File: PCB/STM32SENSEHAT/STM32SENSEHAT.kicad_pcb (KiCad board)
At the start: 2 copper layers, 7.5 x 2 mm, 90 parts, among them IC1 DW01A, J1 USB_B_Micro, J10 Conn_01x01_Pin, J11 Conn_01x02_Pin, J12 Conn_01x04_Pin, J13 Conn_01x04_Pin, J2 Conn_01x24_Socket, J3 Conn_01x24_Socket, J4 Conn_01x05_Pin, J5 Conn_01x24_Pin, J6 Conn_01x10_Pin, J7 Conn_01x04_Socket, J8 Conn_01x24_Pin, J9 Conn_01x05_Socket, Q1 AO3401A, SW1 SW_Push, U1 MCP1700x-330xxTT, U2 TP4056, U3 FT230XQ, U4 BME280, U5 CAT24C256, U6 LTR-303ALS-01, U7 8205A

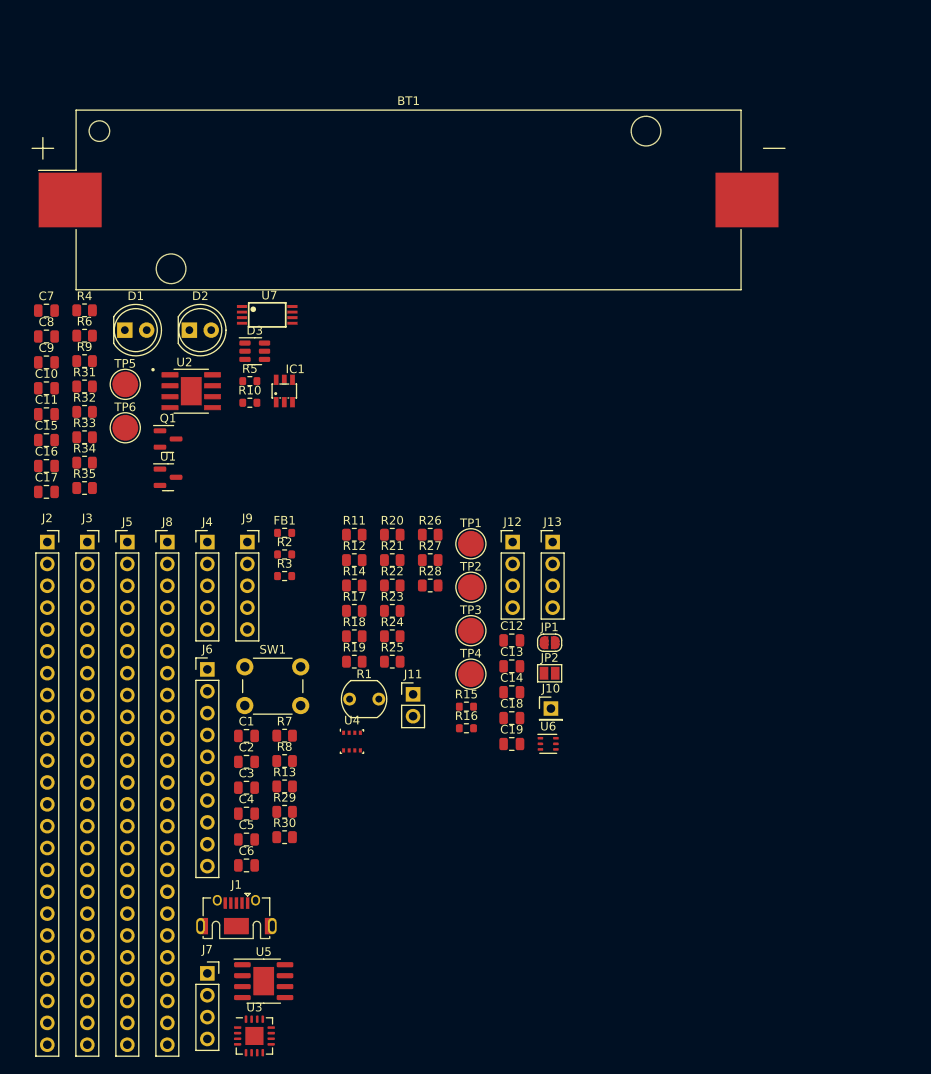
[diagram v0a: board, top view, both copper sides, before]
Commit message: Rework of Power,MCU and Sensor Schematic
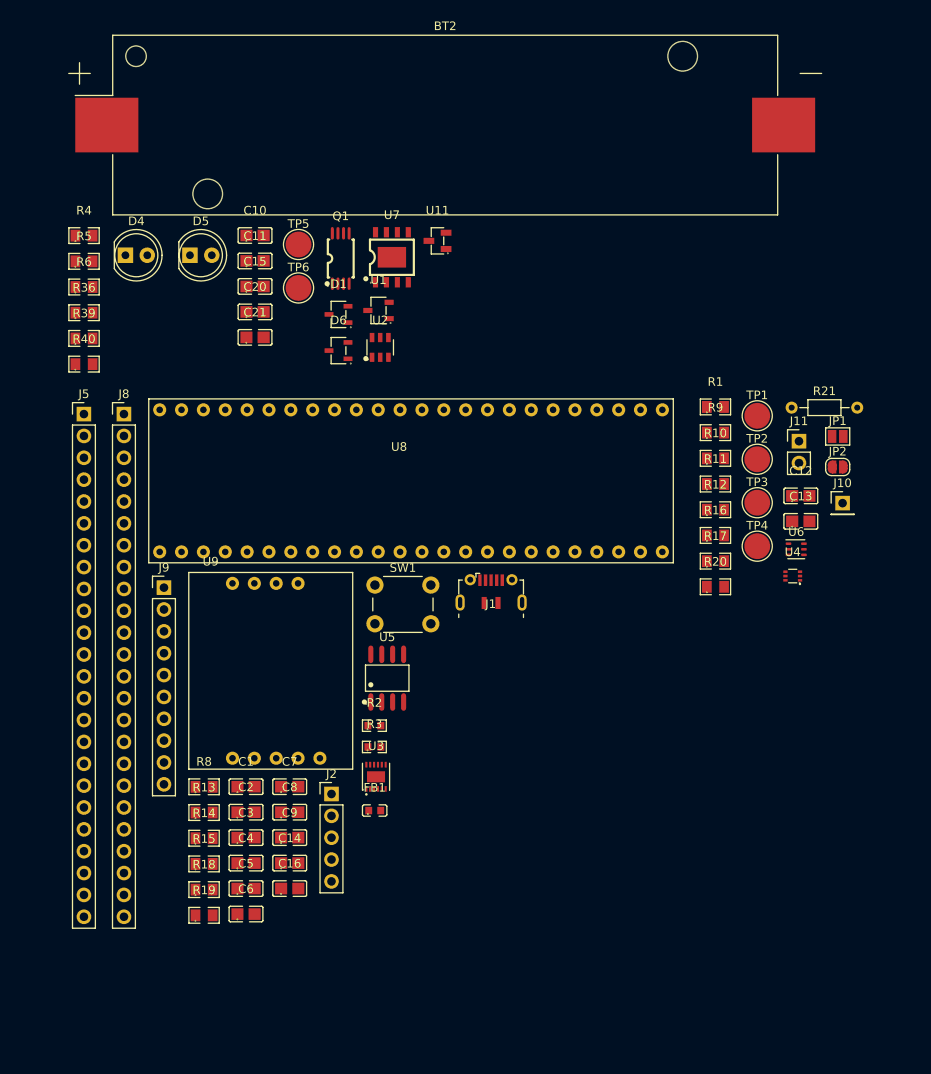
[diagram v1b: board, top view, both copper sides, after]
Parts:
- removed BT1: Battery_Cell, Battery:BatteryHolder_Keystone_1042_1x18650
- removed C17: 1uF, Capacitor_SMD:C_0805_2012Metric
- removed C18, C19: 100nF, Capacitor_SMD:C_0805_2012Metric
- removed D2: LED, LED_THT:LED_D5.0mm
- removed D3: D_Schottky, Package_TO_SOT_SMD:TSOT-23-6
- removed IC1: DW01A, DW01A:SOT23-6
- removed J12, J13: Conn_01x04_Pin, Connector_PinHeader_2.54mm:PinHeader_1x04_P2.54mm_Vertical
- removed J3: Conn_01x24_Socket, Connector_PinSocket_2.54mm:PinSocket_1x24_P2.54mm_Vertical
- removed J4: Conn_01x05_Pin, Connector_PinHeader_2.54mm:PinHeader_1x05_P2.54mm_Vertical
- removed J6: Conn_01x10_Pin, Connector_PinHeader_2.54mm:PinHeader_1x10_P2.54mm_Vertical
- removed J7: Conn_01x04_Socket, Connector_PinSocket_2.54mm:PinSocket_1x04_P2.54mm_Vertical
- removed R22, R23, R24, R25, R26, R27, R28, R29, R30, R31, R32, R33, R34: 0R, Resistor_SMD:R_0805_2012Metric
- removed R35, R7: 10k, Resistor_SMD:R_0805_2012Metric
- added BT2: Battery_Cell, Battery:BatteryHolder_Keystone_1042_1x18650, F.Cu at (147.5, 37.5)
- added C20: 10uF, JLCfootprint:C0805, F.Cu at (125.4, 59.2)
- added C21: 10uF, JLCfootprint:C0805, F.Cu at (125.4, 62.2)
- added D4: LED, LED_THT:LED_D5.0mm, F.Cu at (110.3, 52.6)
- added D5: LED, LED_THT:LED_D5.0mm, F.Cu at (117.8, 52.6)
- added D6: D_Schottky, JLCfootprint:SOT-23-3_L3.0-W1.7-P0.95-LS2.9-BR, F.Cu at (135.1, 63.7)
- added R36: 10k, JLCfootprint:R0805, F.Cu at (105.5, 59.3)
- added R39: 0R, JLCfootprint:R0805, F.Cu at (105.5, 62.3)
- added R40: 1k0, JLCfootprint:R0805, F.Cu at (105.5, 65.3)
- added U11: AO3401A_C306862, JLCfootprint:SOT-23-3_L2.9-W1.3-P1.90-LS2.4-BR, F.Cu at (146.6, 51.0)
- added U8: ~, footprints:STM32F051C6T6, F.Cu at (142.3, 81.0)
- added U9: STLINK_UCT, footprints:STLINK_UCT, F.Cu at (126.6, 100.9)
- C1, C10, C11, C2, C3, C4, C5, C6, C9: footprint Capacitor_SMD:C_0805_2012Metric -> JLCfootprint:C0805
- C12: value 100nF -> 1uF; footprint Capacitor_SMD:C_0805_2012Metric -> JLCfootprint:C0805
- C13: value 100nF -> 10nF; footprint Capacitor_SMD:C_0805_2012Metric -> JLCfootprint:C0805
- C14, C15: value 1uF -> 10nF; footprint Capacitor_SMD:C_0805_2012Metric -> JLCfootprint:C0805
- C16: value 1uF -> 4.7uF; footprint Capacitor_SMD:C_0805_2012Metric -> JLCfootprint:C0805
- C7: value 10uF -> 1uF; footprint Capacitor_SMD:C_0805_2012Metric -> JLCfootprint:C0805
- C8: value 10uF -> 100nF; footprint Capacitor_SMD:C_0805_2012Metric -> JLCfootprint:C0805
- D1: value LED -> D_Schottky; footprint LED_THT:LED_D5.0mm -> JLCfootprint:SOT-23-3_L3.0-W1.7-P0.95-LS2.9-BR
- FB1: footprint Resistor_SMD:R_0603_1608Metric -> JLCfootprint:L0603
- J1: footprint Connector_USB:USB_Micro-AB_Molex_47590-0001 -> footprints:USB_Conn_JLC_LCSC_C404969
- J2: value Conn_01x24_Socket -> Conn_01x05_Pin; footprint Connector_PinSocket_2.54mm:PinSocket_1x24_P2.54mm_Vertical -> Connector_PinHeader_2.54mm:PinHeader_1x05_P2.54mm_Vertical
- J9: value Conn_01x05_Socket -> Conn_01x10_Pin; footprint Connector_PinSocket_2.54mm:PinSocket_1x05_P2.54mm_Vertical -> Connector_PinHeader_2.54mm:PinHeader_1x10_P2.54mm_Vertical
- JP1: footprint Jumper:SolderJumper-2_P1.3mm_Open_RoundedPad1.0x1.5mm -> Jumper:SolderJumper-2_P1.3mm_Open_Pad1.0x1.5mm
- JP2: footprint Jumper:SolderJumper-2_P1.3mm_Open_Pad1.0x1.5mm -> Jumper:SolderJumper-2_P1.3mm_Open_RoundedPad1.0x1.5mm
- Q1: value AO3401A -> FS8205A; footprint Package_TO_SOT_SMD:SOT-23 -> JLCfootprint:TSSOP-8_L4.4-W3.0-P0.65-LS6.4-BL
- R1: value LDR07 -> 0R; footprint OptoDevice:R_LDR_5.1x4.3mm_P3.4mm_Vertical -> JLCfootprint:R0805
- R10: value 1k -> 0R; footprint Resistor_SMD:R_0603_1608Metric -> JLCfootprint:R0805
- R11, R12: value 4k7 -> 0R; footprint Resistor_SMD:R_0805_2012Metric -> JLCfootprint:R0805
- R13, R8: value 1.5k -> 0R; footprint Resistor_SMD:R_0805_2012Metric -> JLCfootprint:R0805
- R14: footprint Resistor_SMD:R_0805_2012Metric -> JLCfootprint:R0805
- R15: value 1k0 -> 4k7; footprint Resistor_SMD:R_0603_1608Metric -> JLCfootprint:R0805
- R16: value 1k0 -> 0R; footprint Resistor_SMD:R_0603_1608Metric -> JLCfootprint:R0805
- R17: value 10k -> 0R; footprint Resistor_SMD:R_0805_2012Metric -> JLCfootprint:R0805
- R18: value 0R -> 4k7; footprint Resistor_SMD:R_0805_2012Metric -> JLCfootprint:R0805
- R19, R20: value 0R -> 10k; footprint Resistor_SMD:R_0805_2012Metric -> JLCfootprint:R0805
- R2, R3: footprint Resistor_SMD:R_0603_1608Metric -> JLCfootprint:R0603
- R21: value 0R -> LDR07; footprint Resistor_SMD:R_0805_2012Metric -> Resistor_THT:R_Axial_DIN0204_L3.6mm_D1.6mm_P7.62mm_Horizontal
- R4: value 0.4R -> 1k0; footprint Resistor_SMD:R_0805_2012Metric -> JLCfootprint:R0805
- R5: value 1k0 -> 10k; footprint Resistor_SMD:R_0603_1608Metric -> JLCfootprint:R0805
- R6: value 10k -> 100R; footprint Resistor_SMD:R_0805_2012Metric -> JLCfootprint:R0805
- R9: value 100R -> 0R; footprint Resistor_SMD:R_0805_2012Metric -> JLCfootprint:R0805
- U1: footprint Package_TO_SOT_SMD:SOT-23 -> JLCfootprint:SOT-23-3_L2.9-W1.6-P1.90-LS2.8-BR
- U2: value TP4056 -> ~; footprint TP4056:SOP127P600X175-9N -> JLCfootprint:SOT-23-6_L2.9-W1.6-P0.95-LS2.8-BL
- U3: value FT230XQ -> FT234XD-R; footprint Package_DFN_QFN:QFN-16-1EP_4x4mm_P0.65mm_EP2.1x2.1mm -> JLCfootprint:DFN-12_L3.0-W3.0-P0.45-BL-EP
- U4: value BME280 -> TMP102xxDRL; footprint Package_LGA:Bosch_LGA-8_2.5x2.5mm_P0.65mm_ClockwisePinNumbering -> JLCfootprint:SOT-563_L1.6-W1.2-P0.50-LS1.6-BR
- U5: footprint Package_SO:SOIC-8-1EP_3.9x4.9mm_P1.27mm_EP2.41x3.3mm -> JLCfootprint:SOIC-8_L4.9-W3.9-P1.27-LS6.0-BL
- U7: value 8205A -> ~; footprint 8205A:TSSOP8 -> JLCfootprint:ESOP-8_L4.9-W3.9-P1.27-LS6.0-BL-EP
- moved R9 73.8 mm to (178.9, 73.3)
- moved C7 62.1 mm to (129.4, 114.4)
- moved C8 62.1 mm to (129.4, 117.4)
- moved C9 62.0 mm to (129.4, 120.3)
- moved C16 56.7 mm to (129.4, 126.3)
- moved U4 54.7 mm to (187.9, 89.9)
- moved R10 54.5 mm to (178.9, 76.2)
- moved R1 54.4 mm to (178.9, 70.3)
- moved J11 53.6 mm to (188.6, 74.3)
- moved R21 49.7 mm to (187.7, 70.4)
- moved J1 47.3 mm to (152.8, 93.7)
- moved J2 44.1 mm to (134.3, 115.3)
- moved R11 42.4 mm to (178.9, 79.2)
- moved R12 42.4 mm to (178.9, 82.2)
- moved R17 42.4 mm to (178.9, 88.2)
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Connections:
- C12 pad 1: GND -> Net-(JP1-A)
- C12 pad 2: Net-(U4-VDDIO) -> GND
- C13 pad 1: GND -> 3V3
- C13 pad 2: Net-(U4-VDD) -> GND
- C14 pad 1: Net-(JP2-A) -> 3V3
- C15 pad 1: 3V3 -> Net-(U2-VDD)
- C15 pad 2: GND -> Net-(D1-K)
- C2 pad 1: /MCU MODULE/VBUS -> /MCU MODULE/PB0
- C7 pad 1: /MCU MODULE/PA4 -> 3V3
- C8 pad 1: Net-(C8-Pad1) -> 3V3
- C9 pad 1: Net-(IC1-VCC) -> 3V3
- D1 pad 2: Net-(D1-A) -> Net-(BT2--)
- FB1 pad 2: /MCU MODULE/VBUS -> /MCU MODULE/PB0
- J1 pad 1: /MCU MODULE/VBUS -> /MCU MODULE/PB0
- J2 pad 1: 3V3 -> /MCU MODULE/PB0
- J2 pad 2: /MCU MODULE/PC13 -> /MCU MODULE/USB_DN
- J2 pad 3: /MCU MODULE/PC14 -> /MCU MODULE/USB_DP
- J2 pad 4: /MCU MODULE/PC15 -> GND
- J2 pad 5: /MCU MODULE/PF0 -> GND
- J5 pad 1: /MCU MODULE/VDD -> 3V3
- J5 pad 10: /MCU MODULE/PB3 -> /MCU MODULE/PA0
- J5 pad 11: /MCU MODULE/PA15 -> /MCU MODULE/PA1
- J5 pad 12: /MCU MODULE/PA14 -> /MCU MODULE/PA2
- J5 pad 13: /MCU MODULE/PF7 -> /MCU MODULE/PA3
- J5 pad 14: /MCU MODULE/PF6 -> /MCU MODULE/PA4
- J5 pad 15: /MCU MODULE/PA13 -> /MCU MODULE/PA5
- J5 pad 16: /MCU MODULE/PA12 -> /MCU MODULE/PA6
- J5 pad 17: /MCU MODULE/PA11 -> /MCU MODULE/PA7
- J5 pad 18: /MCU MODULE/PA10 -> /MCU MODULE/PB0
- J5 pad 19: /MCU MODULE/PA9 -> /MCU MODULE/PB1
- J5 pad 2: GND -> /MCU MODULE/PC13
- J5 pad 20: /MCU MODULE/PA8 -> /MCU MODULE/PB2
- J5 pad 21: /MCU MODULE/PB15 -> /MCU MODULE/PB10
- J5 pad 22: /MCU MODULE/PB14 -> /MCU MODULE/PB11
- J5 pad 23: /MCU MODULE/PB13 -> GND
- J5 pad 24: /MCU MODULE/PB12 -> 3V3
- J5 pad 3: /MCU MODULE/PB9 -> /MCU MODULE/PC14
- J5 pad 4: /MCU MODULE/PB8 -> /MCU MODULE/PC15
- J5 pad 5: /MCU MODULE/BOOT -> /MCU MODULE/PF0
- J5 pad 6: /MCU MODULE/PB7 -> /MCU MODULE/PF1
- J5 pad 7: /MCU MODULE/PB6 -> /MCU MODULE/NRST
- J5 pad 8: /MCU MODULE/PB5 -> GND
- J5 pad 9: /MCU MODULE/PB4 -> 3V3
- J8 pad 1: /MCU MODULE/VBAT -> 3V3
- J8 pad 10: /MCU MODULE/PA0 -> /MCU MODULE/PB3
- J8 pad 11: /MCU MODULE/PA1 -> /MCU MODULE/PA15
- J8 pad 12: /MCU MODULE/PA2 -> /MCU MODULE/PA14
- J8 pad 13: /MCU MODULE/PA3 -> /MCU MODULE/PF7
- J8 pad 14: /MCU MODULE/PA4 -> /MCU MODULE/PF6
- J8 pad 15: /MCU MODULE/ANALOG DATA READ -> /MCU MODULE/PA13
- J8 pad 16: /MCU MODULE/PA6 -> /MCU MODULE/PA12
- J8 pad 17: /MCU MODULE/PA7 -> /MCU MODULE/PA11
- J8 pad 18: /MCU MODULE/PB0 -> /MCU MODULE/PA10
- J8 pad 19: /MCU MODULE/PB1 -> /MCU MODULE/PA9
- J8 pad 2: /MCU MODULE/PC13 -> GND
- J8 pad 20: /MCU MODULE/PB2 -> /MCU MODULE/PA8
- J8 pad 21: /MCU MODULE/PB10 -> /MCU MODULE/PB15
- J8 pad 22: /MCU MODULE/PB11 -> /MCU MODULE/PB14
- J8 pad 23: GND -> /MCU MODULE/PB13
- J8 pad 24: /MCU MODULE/VDD -> /MCU MODULE/PB12
- J8 pad 3: /MCU MODULE/PC14 -> /MCU MODULE/PB9
- J8 pad 4: /MCU MODULE/PC15 -> /MCU MODULE/PB8
- J8 pad 5: /MCU MODULE/PF0 -> /MCU MODULE/BOOT
- J8 pad 6: /MCU MODULE/PF1 -> /MCU MODULE/PB7
- J8 pad 7: /MCU MODULE/NRST -> /MCU MODULE/PB6
- J8 pad 8: GND -> /MCU MODULE/PB5
- J8 pad 9: /MCU MODULE/VDDA -> /MCU MODULE/PB4
- J9 pad 2: 3V3 -> /MCU MODULE/PA5
- J9 pad 3: /MCU MODULE/USB_DP -> /MCU MODULE/PB7
- J9 pad 4: /MCU MODULE/USB_DN -> /MCU MODULE/PB6
- J9 pad 5: GND -> unconnected-(J9-Pin_5-Pad5)
- JP1 pad 1: /MCU MODULE/ANALOG DATA READ -> Net-(JP1-A)
- JP1 pad 2: Net-(J10-Pin_1) -> 3V3
- JP2 pad 1: Net-(JP2-A) -> /MCU MODULE/PA5
- JP2 pad 2: 3V3 -> Net-(J10-Pin_1)
- Q1 pad 1: 5VUSB -> unconnected-(Q1-Pad1)
- Q1 pad 2: /POWER MANAGEMENT MODULE/LOAD_PWR -> Net-(D1-K)
- Q1 pad 3: /MCU MODULE/PA4 -> Net-(D1-K)
- R1 pad 1: /MCU MODULE/ANALOG DATA READ -> Net-(U4-V+)
- R1 pad 2: GND -> 3V3
- R10 pad 1: Net-(IC1-CS) -> Net-(U4-SCL)
- R10 pad 2: /POWER MANAGEMENT MODULE/S2 -> /MCU MODULE/PB6
- R11 pad 1: /MCU MODULE/PF6 -> Net-(U6-VDD)
- R11 pad 2: Net-(U4-VDDIO) -> Net-(JP1-A)
- R12 pad 1: /MCU MODULE/PF7 -> GND
- R12 pad 2: Net-(U4-VDDIO) -> Net-(U6-GND)
- R13 pad 1: 3V3 -> /MCU MODULE/PB7
- R13 pad 2: /MCU MODULE/PF7 -> Net-(U5-SDA)
- R14 pad 1: Net-(U4-SCK) -> 3V3
- R14 pad 2: /MCU MODULE/PF7 -> Net-(U5-VCC)
- R15 pad 1: Net-(JP2-A) -> /MCU MODULE/PB7
- R15 pad 2: /MCU MODULE/PF6 -> 3V3
- R16 pad 1: Net-(JP2-A) -> Net-(U6-SDA)
- R16 pad 2: /MCU MODULE/PF7 -> /MCU MODULE/PB7
- R17 pad 1: 3V3 -> Net-(U6-SCL)
- R17 pad 2: /MCU MODULE/ANALOG DATA READ -> /MCU MODULE/PB6
- R18 pad 1: Net-(U4-SDI) -> /MCU MODULE/PB6
- R18 pad 2: /MCU MODULE/PF6 -> 3V3
- R19 pad 1: Net-(U4-CSB) -> /MCU MODULE/BOOT
- R19 pad 2: Net-(U4-VDDIO) -> GND
- R20 pad 1: Net-(U4-VDDIO) -> 3V3
- R20 pad 2: 3V3 -> /MCU MODULE/PA5
- R21 pad 1: Net-(U4-VDD) -> /MCU MODULE/PA5
- R21 pad 2: 3V3 -> GND
- R4 pad 1: 5VUSB -> Net-(U2-CS)
- R4 pad 2: Net-(C8-Pad1) -> GND
- R5 pad 1: Net-(C8-Pad1) -> 5VUSB
- R5 pad 2: Net-(D1-A) -> GND
- R6 pad 1: /POWER MANAGEMENT MODULE/PROG -> Net-(U2-VDD)
- R6 pad 2: GND -> /POWER MANAGEMENT MODULE/BATT+
- R8 pad 1: 3V3 -> Net-(U5-SCL)
- R8 pad 2: Net-(R30-Pad2) -> /MCU MODULE/PB6
- R9 pad 1: /MCU MODULE/PA4 -> Net-(U4-SDA)
- R9 pad 2: Net-(IC1-VCC) -> /MCU MODULE/PB7
- TP1 pad 1: /MCU MODULE/PF7 -> /MCU MODULE/PB7
- TP2 pad 1: /MCU MODULE/PF6 -> /MCU MODULE/PB6
- TP3 pad 1: /MCU MODULE/PF6 -> /MCU MODULE/PB7
- TP4 pad 1: /MCU MODULE/PF7 -> /MCU MODULE/PB6
- U2 pad 1: unconnected-(U2-TEMP-Pad1) -> Net-(U2-OD)
- U2 pad 2: /POWER MANAGEMENT MODULE/PROG -> Net-(U2-CS)
- U2 pad 3: GND -> Net-(U2-OC)
- U2 pad 4: 5VUSB -> unconnected-(U2-TD-Pad4)
- U2 pad 5: /MCU MODULE/PA4 -> Net-(U2-VDD)
- U3 pad 1: Net-(U3-3V3OUT) -> Net-(U3-USBDM)
- U3 pad 10: 5VUSB -> /MCU MODULE/PA9
- U3 pad 12: unconnected-(U3-CBUS0-Pad12) -> Net-(U3-USBDP)
- U3 pad 2: /MCU MODULE/PA10 -> Net-(U3-3V3OUT)
- U3 pad 3: GND -> Net-(U3-3V3OUT)
- U3 pad 4: unconnected-(U3-~{CTS}-Pad4) -> 5VUSB
- U3 pad 5: unconnected-(U3-CBUS2-Pad5) -> GND
- U3 pad 6: Net-(U3-USBDP) -> unconnected-(U3-CBUS0-Pad6)
- U3 pad 7: Net-(U3-USBDM) -> /MCU MODULE/PA10
- U3 pad 8: Net-(U3-3V3OUT) -> unconnected-(U3-RTS#-Pad8)
- U4 pad 1: /SENSOR MODULE/1 -> Net-(U4-SCL)
- U4 pad 2: Net-(U4-CSB) -> GND
- U4 pad 3: Net-(U4-SDI) -> unconnected-(U4-ALERT-Pad3)
- U4 pad 4: Net-(U4-SCK) -> GND
- U4 pad 5: Net-(U4-SDO) -> Net-(U4-V+)
- U4 pad 6: Net-(U4-VDDIO) -> Net-(U4-SDA)
- U5 pad 5: /MCU MODULE/PF6 -> Net-(U5-SDA)
- U5 pad 8: 3V3 -> Net-(U5-VCC)
- U7 pad 1: Net-(U7-D1) -> GND
- U7 pad 2: Net-(U7-S1) -> /POWER MANAGEMENT MODULE/PROG
- U7 pad 3: Net-(U7-S1_2) -> GND
- U7 pad 4: /POWER MANAGEMENT MODULE/OD -> 5VUSB
- U7 pad 5: /POWER MANAGEMENT MODULE/OC -> /POWER MANAGEMENT MODULE/BATT+
- U7 pad 8: Net-(U7-D1) -> 5VUSB
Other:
- board outline removed

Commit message: PCB draft
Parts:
- added D1: D_Schottky, JLCfootprint:SOT-23-3_L3.0-W1.7-P0.95-LS2.9-BR, F.Cu at (110.2, 107.0)
- C1, C10, C11, C12, C13, C15, C2, C20, C21, C3, C4, C5, C6: footprint JLCfootprint:C0805 -> Capacitor_SMD:C_0805_2012Metric
- C14, C16, C7, C8, C9: footprint JLCfootprint:C0805 -> Capacitor_THT:C_Disc_D5.0mm_W2.5mm_P5.00mm
- R1, R10, R11, R12, R13, R14, R15, R16, R17, R18, R19, R20, R36, R39, R4, R40, R5, R6, R8, R9: footprint JLCfootprint:R0805 -> Resistor_SMD:R_0805_2012Metric
- R2, R3: footprint JLCfootprint:R0603 -> Resistor_SMD:R_0805_2012Metric
- R21: footprint Resistor_THT:R_Axial_DIN0204_L3.6mm_D1.6mm_P7.62mm_Horizontal -> OptoDevice:R_LDR_5.1x4.3mm_P3.4mm_Vertical
- U2: value ~ -> DW01A
- U6: footprint OptoDevice:Lite-On_LTR-303ALS-01 -> JLCfootprint:SOT-363_L2.0-W1.3-P0.65-LS2.1-BL
- U7: value ~ -> TP4056
- moved R19 80.0 mm to (167.0, 65.0)
- moved R8 69.3 mm to (188.3, 122.0), turned to 180 degrees
- moved R15 68.2 mm to (176.5, 86.0)
- moved R18 67.9 mm to (176.5, 89.5)
- moved U9 65.6 mm to (185.8, 72.8), turned to -90 degrees
- moved R13 64.4 mm to (183.7, 121.9)
- moved J9 61.6 mm to (176.4, 94.2)
- moved J8 60.9 mm to (171.0, 68.4)
- moved R14 60.2 mm to (179.2, 127.8), turned to -90 degrees
- moved U11 60.0 mm to (126.0, 107.3)
- moved R5 59.0 mm to (118.1, 111.0), turned to 180 degrees
- moved J1 56.3 mm to (120.1, 139.5)
- moved Q1 56.2 mm to (118.5, 106.6), turned to -90 degrees
- moved R6 54.7 mm to (110.1, 110.8), turned to 180 degrees
- moved C8 52.8 mm to (150.9, 69.1)
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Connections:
- BT2 pad 1: /POWER MANAGEMENT MODULE/BATT+ -> Net-(BT2-+)
- C15 pad 2: Net-(D1-K) -> Net-(BT2--)
- Q1 pad 2: Net-(D1-K) -> Net-(BT2--)
- Q1 pad 3: Net-(D1-K) -> Net-(BT2--)
- U2 pad 6: Net-(D1-K) -> Net-(BT2--)
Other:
- board outline added: 100 x 100 mm

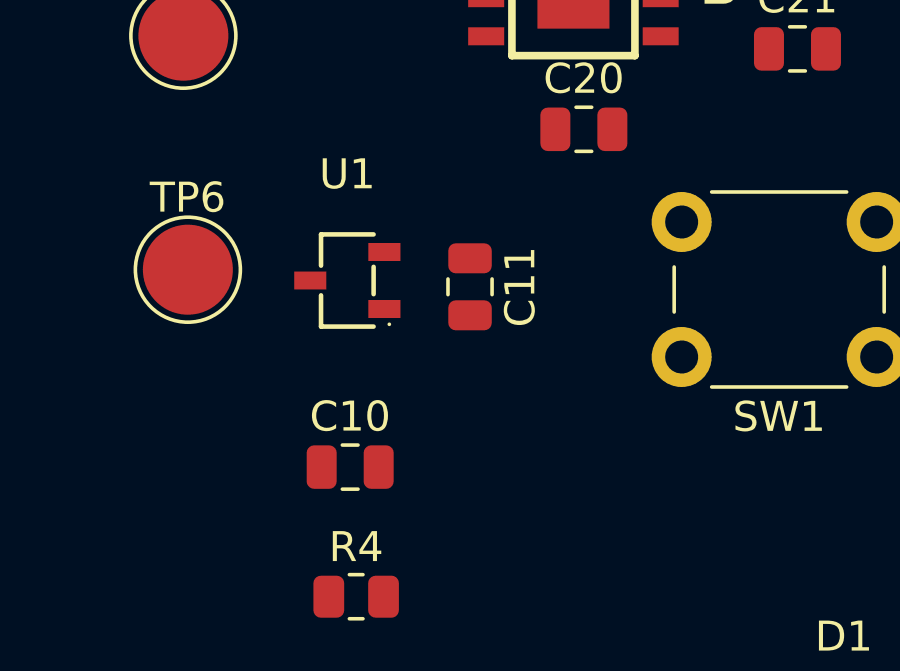
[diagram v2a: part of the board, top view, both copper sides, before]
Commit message: Changed the footprint of cpacitors C10 and C11 to C_disc"
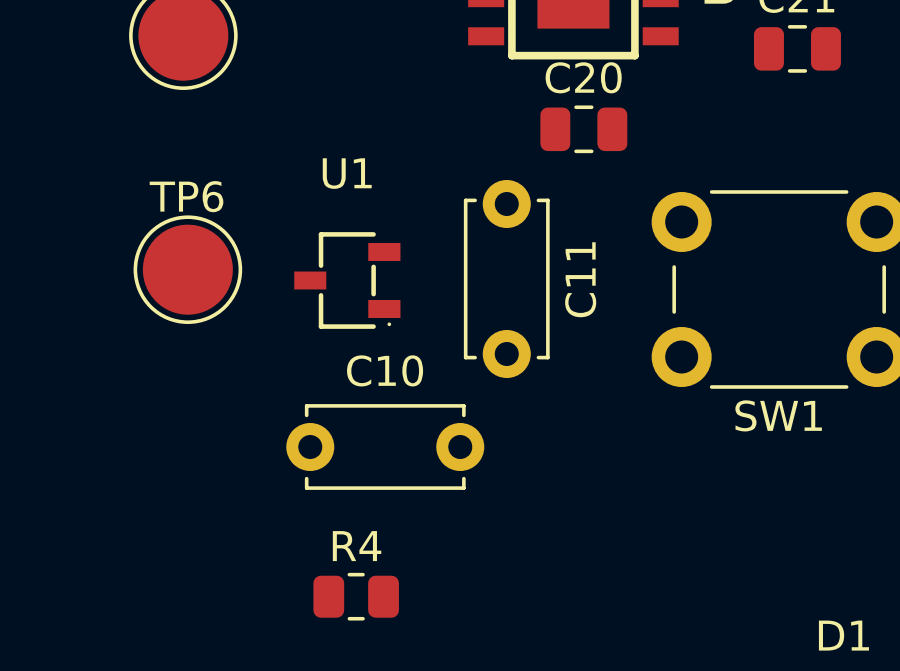
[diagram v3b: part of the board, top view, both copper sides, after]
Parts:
- C10, C11: footprint Capacitor_SMD:C_0805_2012Metric -> Capacitor_THT:C_Disc_D5.0mm_W2.5mm_P5.00mm
- moved C11 3.02 mm to (120.3, 83.7)
- moved C10 1.49 mm to (113.7, 91.8)

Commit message: Update
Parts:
- moved TP1 15.0 mm to (181.7, 96.5)
- moved FB1 14.6 mm to (111.9, 135.4), turned to 180 degrees
- moved C10 8.46 mm to (120.5, 96.9), turned to 90 degrees
- moved R6 8.08 mm to (109.3, 102.8)
- moved C6 5.13 mm to (111.8, 126.5)
- moved C2 4.76 mm to (112.0, 137.8)
- moved C4 4.19 mm to (111.7, 122.9)
- moved C5 4.19 mm to (111.7, 120.0)
- moved C20 3.50 mm to (126.4, 81.4)
- moved R2 3.12 mm to (117.8, 126.2)
- moved R3 2.89 mm to (117.9, 129.4)
- moved C1 2.82 mm to (111.9, 133.2)
- moved J2 2.21 mm to (118.7, 119.3)
- moved R4 2.11 mm to (116.0, 94.8), turned to 90 degrees
- moved R5 1.64 mm to (118.7, 112.5)
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
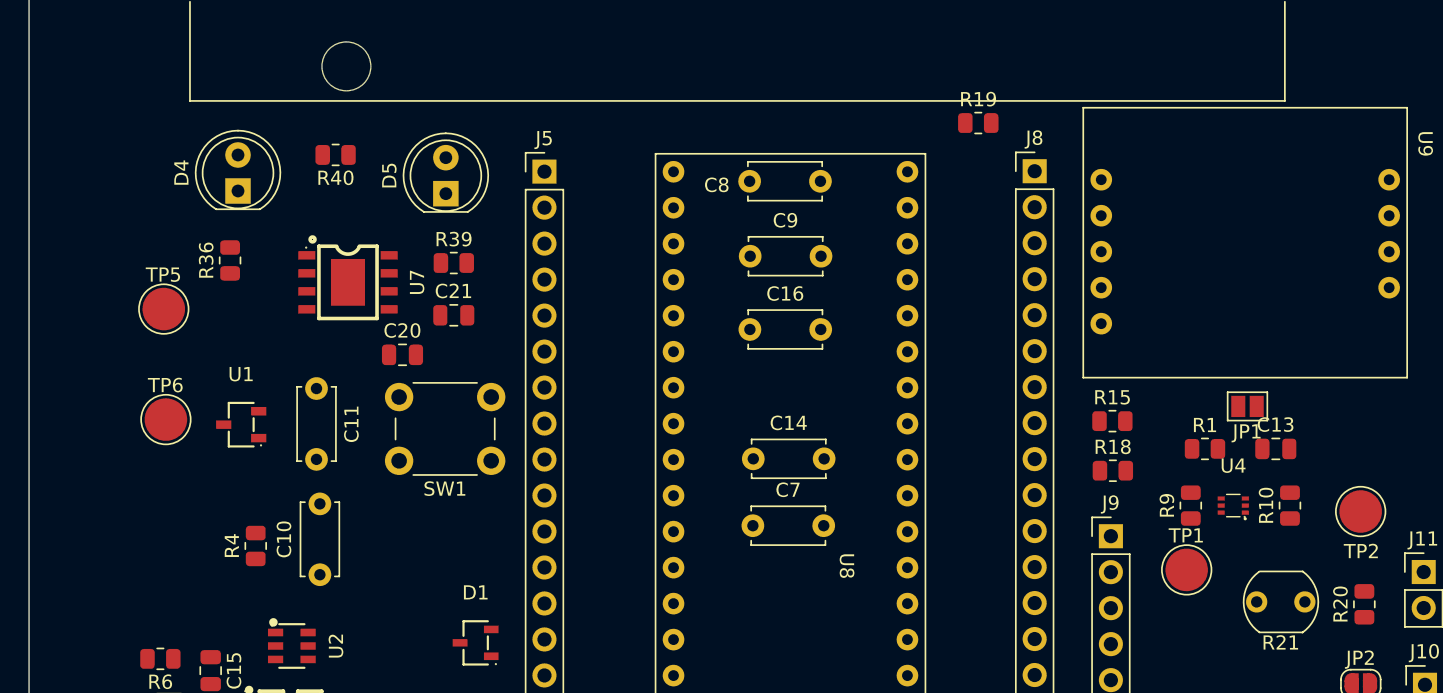
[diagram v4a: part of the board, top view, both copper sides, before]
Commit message: OScillator added
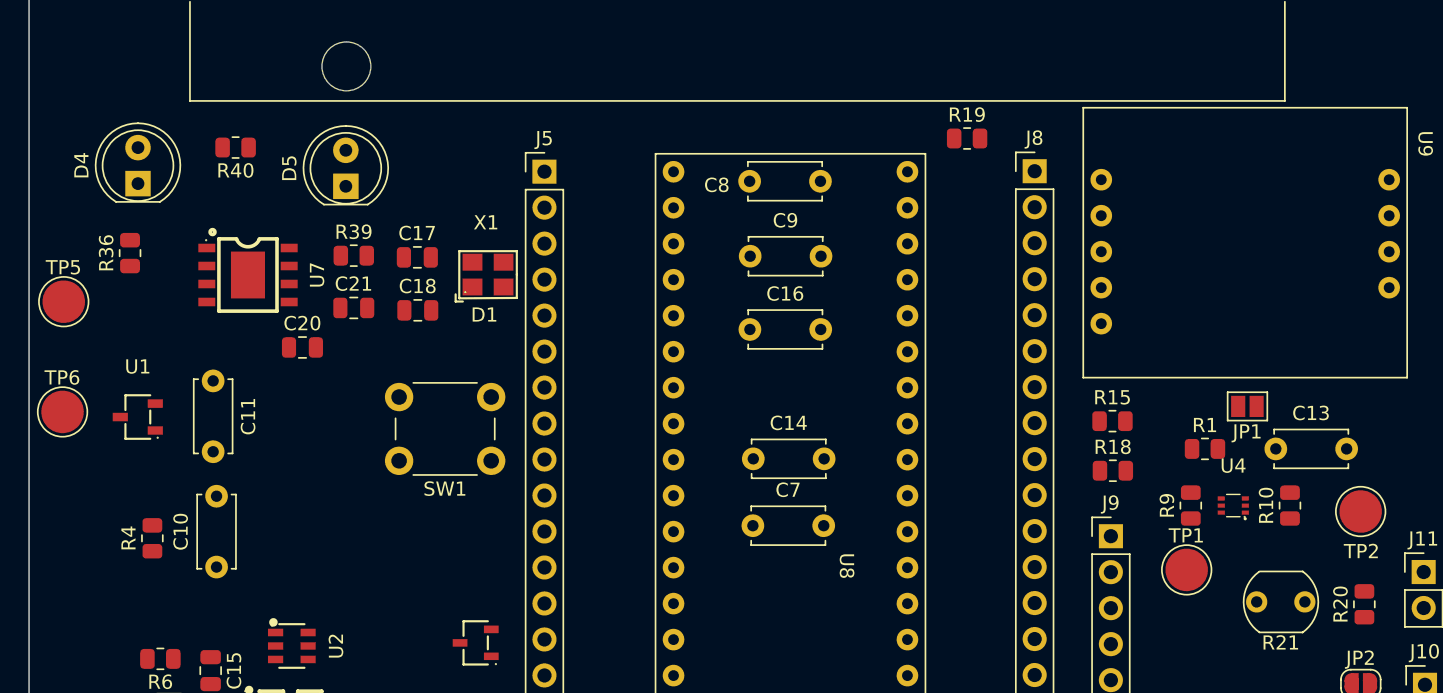
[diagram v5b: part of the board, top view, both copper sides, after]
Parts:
- added C17: 10nF, Capacitor_SMD:C_0805_2012Metric, F.Cu at (127.4, 74.5)
- added C18: 10nF, Capacitor_SMD:C_0805_2012Metric, F.Cu at (127.4, 78.2)
- added X1: XXDCELNANF-8MHZ, JLCfootprint:OSC-SMD_4P-L3.2-W2.5-BL, F.Cu at (132.4, 75.7)
- C13: footprint Capacitor_SMD:C_0805_2012Metric -> Capacitor_THT:C_Disc_D5.0mm_W2.5mm_P5.00mm
- C15: value 10nF -> 100nF
- moved C11 7.31 mm to (113.0, 83.2)
- moved TP6 7.31 mm to (102.4, 85.4)
- moved C10 7.31 mm to (113.2, 96.3)
- moved R4 7.31 mm to (108.7, 94.3)
- moved U1 7.31 mm to (107.7, 85.8)
- moved U7 7.08 mm to (115.5, 75.7)
- moved C20 7.08 mm to (119.3, 80.8)
- moved D4 7.08 mm to (107.7, 69.3)
- moved R36 7.08 mm to (107.1, 74.2)
- moved R40 7.08 mm to (114.6, 66.7)
- moved TP5 7.08 mm to (102.5, 77.6)
- moved C21 7.08 mm to (122.9, 78.0)
- moved D5 7.08 mm to (122.4, 69.5)
- moved R39 7.08 mm to (122.9, 74.4)
- moved R19 1.35 mm to (166.2, 66.1)
